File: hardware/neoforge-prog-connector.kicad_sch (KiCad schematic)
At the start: 1 part, among them J1 AES_CN5_PROG

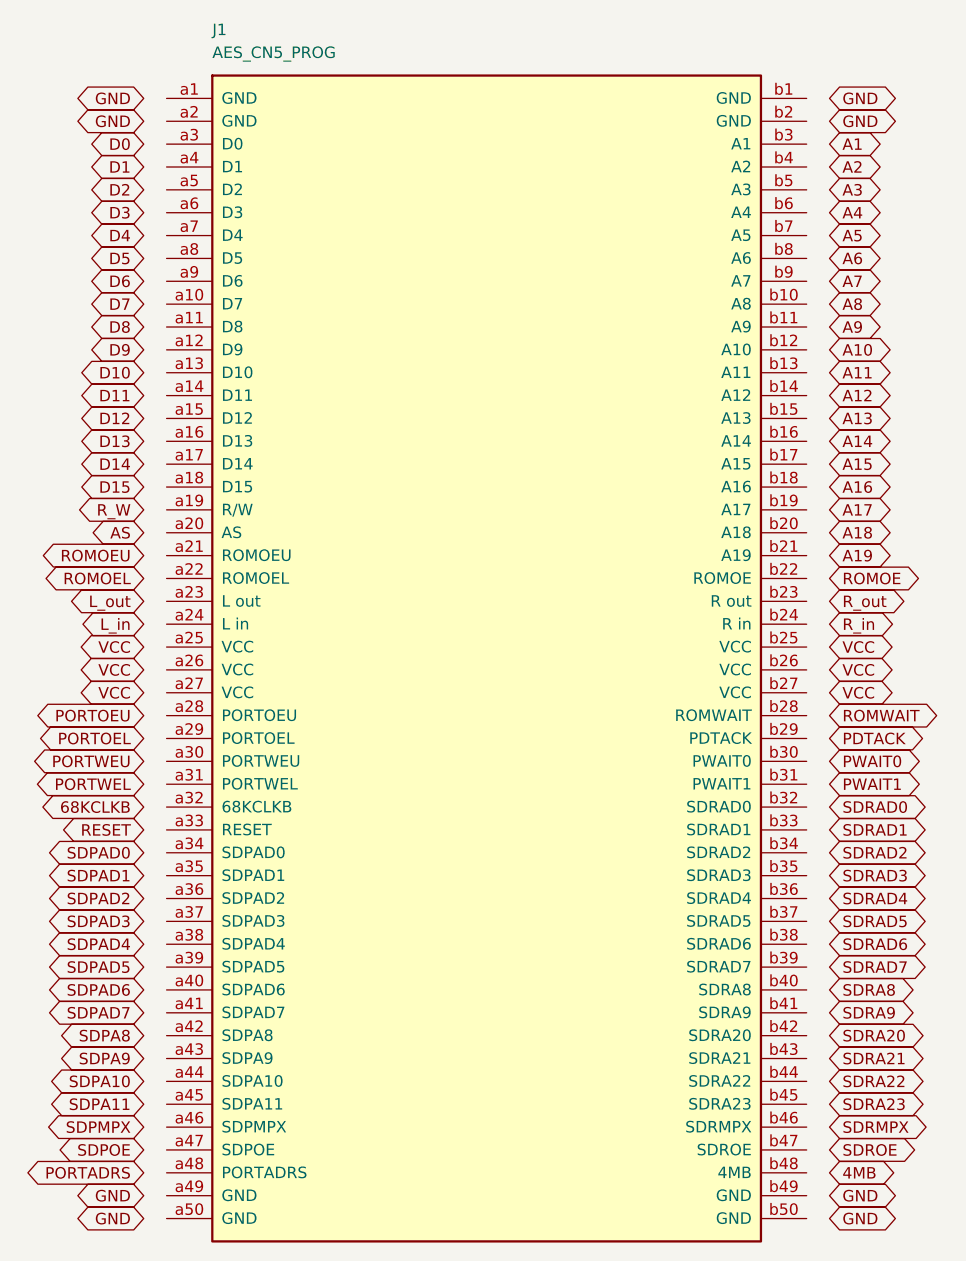
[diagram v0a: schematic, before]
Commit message: hardware: connector netlist verified 100/100
Exported from KiCad and checked back against the pinout CSV:

    J1 -> PROG CN5
      identified from the symbol's Value
      100/100 pins match the pinout
      no issues

The chain closes with nothing transcribed by hand: a CSV verified against
two independent sources, a symbol generated from it, a sheet generated
from it, KiCad's netlist exported from that, and the checker agreeing.

Three bugs were caught on the way and all three were in the tooling, not
the data - the Y-axis inversion between symbol and sheet space, an empty
lib_symbols that rendered a placeholder, and a label offset that produced
a sheet which looked correct and connected nothing. The last is the one
netcheck exists for.

Roadmap: Phase 7's connector item is electrically done, mechanically
open. The footprint still needs measuring off a real cartridge.
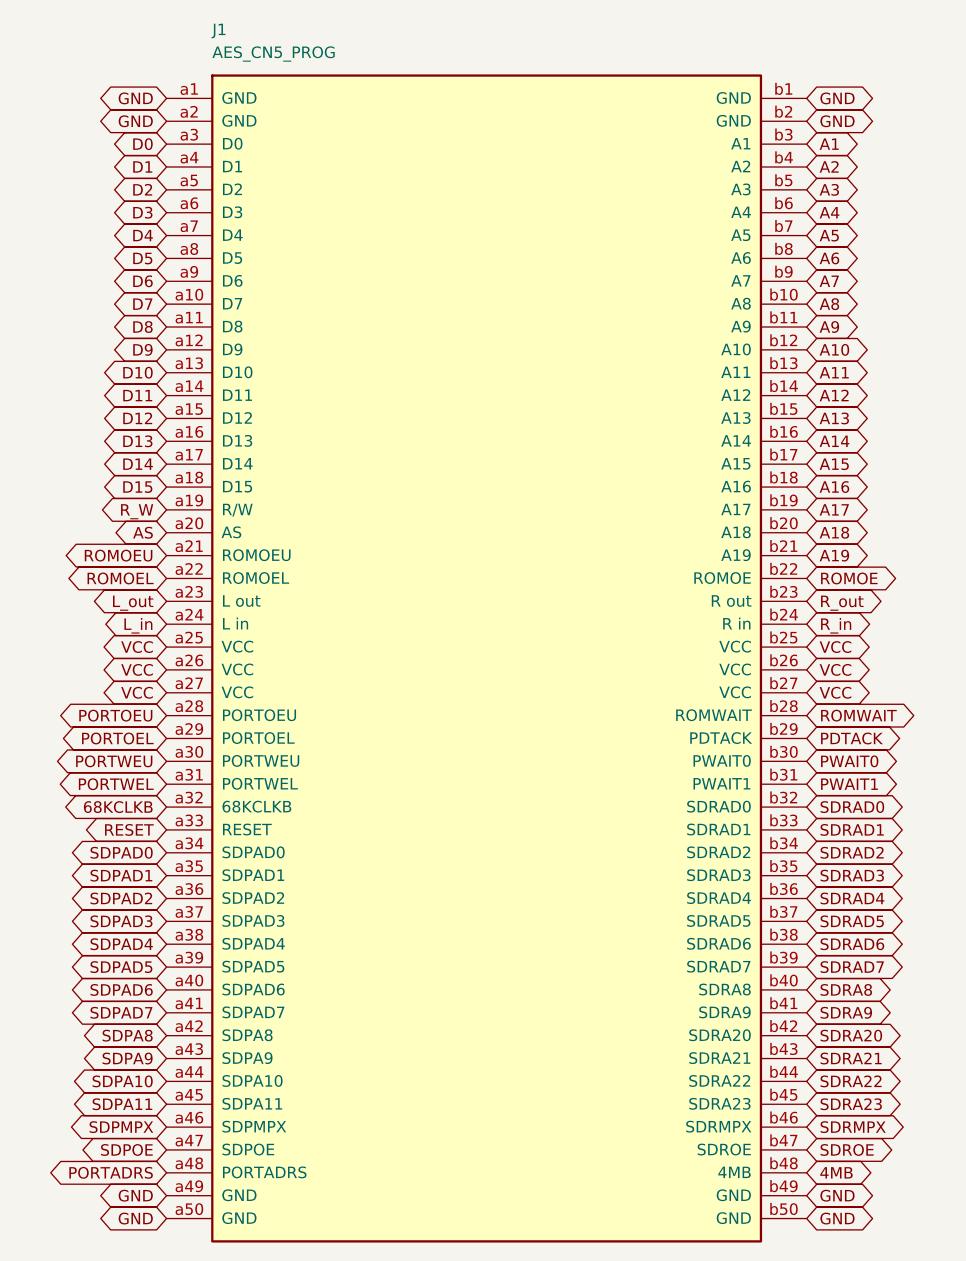
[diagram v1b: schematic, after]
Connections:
- net 4MB: now also J1.b48 (4MB)
- net 68KCLKB: now also J1.a32 (68KCLKB)
- net A1: now also J1.b3 (A1)
- net A10: now also J1.b12 (A10)
- net A11: now also J1.b13 (A11)
- net A12: now also J1.b14 (A12)
- net A13: now also J1.b15 (A13)
- net A14: now also J1.b16 (A14)
- net A15: now also J1.b17 (A15)
- net A16: now also J1.b18 (A16)
- net A17: now also J1.b19 (A17)
- net A18: now also J1.b20 (A18)
- net A19: now also J1.b21 (A19)
- net A2: now also J1.b4 (A2)
- net A3: now also J1.b5 (A3)
- net A4: now also J1.b6 (A4)
- net A5: now also J1.b7 (A5)
- net A6: now also J1.b8 (A6)
- net A7: now also J1.b9 (A7)
- net A8: now also J1.b10 (A8)
- net A9: now also J1.b11 (A9)
- net AS: now also J1.a20 (AS)
- net D0: now also J1.a3 (D0)
- net D1: now also J1.a4 (D1)
- net D10: now also J1.a13 (D10)
- net D11: now also J1.a14 (D11)
- net D12: now also J1.a15 (D12)
- net D13: now also J1.a16 (D13)
- net D14: now also J1.a17 (D14)
- net D15: now also J1.a18 (D15)
- net D2: now also J1.a5 (D2)
- net D3: now also J1.a6 (D3)
- net D4: now also J1.a7 (D4)
- net D5: now also J1.a8 (D5)
- net D6: now also J1.a9 (D6)
- net D7: now also J1.a10 (D7)
- net D8: now also J1.a11 (D8)
- net D9: now also J1.a12 (D9)
- net GND: now also J1.a1 (GND), J1.a2 (GND), J1.a49 (GND), J1.a50 (GND), J1.b1 (GND), J1.b2 (GND), J1.b49 (GND), J1.b50 (GND)
- net L_in: now also J1.a24 (L in)
- net L_out: now also J1.a23 (L out)
- net PDTACK: now also J1.b29 (PDTACK)
- net PORTADRS: now also J1.a48 (PORTADRS)
- net PORTOEL: now also J1.a29 (PORTOEL)
- net PORTOEU: now also J1.a28 (PORTOEU)
- net PORTWEL: now also J1.a31 (PORTWEL)
- net PORTWEU: now also J1.a30 (PORTWEU)
- net PWAIT0: now also J1.b30 (PWAIT0)
- net PWAIT1: now also J1.b31 (PWAIT1)
- net RESET: now also J1.a33 (RESET)
- net ROMOE: now also J1.b22 (ROMOE)
- net ROMOEL: now also J1.a22 (ROMOEL)
- net ROMOEU: now also J1.a21 (ROMOEU)
- net ROMWAIT: now also J1.b28 (ROMWAIT)
- net R_W: now also J1.a19 (R/W)
- net R_in: now also J1.b24 (R in)
- net R_out: now also J1.b23 (R out)
- net SDPA10: now also J1.a44 (SDPA10)
- net SDPA11: now also J1.a45 (SDPA11)
- net SDPA8: now also J1.a42 (SDPA8)
- net SDPA9: now also J1.a43 (SDPA9)
- net SDPAD0: now also J1.a34 (SDPAD0)
- net SDPAD1: now also J1.a35 (SDPAD1)
- net SDPAD2: now also J1.a36 (SDPAD2)
- net SDPAD3: now also J1.a37 (SDPAD3)
- net SDPAD4: now also J1.a38 (SDPAD4)
- net SDPAD5: now also J1.a39 (SDPAD5)
- net SDPAD6: now also J1.a40 (SDPAD6)
- net SDPAD7: now also J1.a41 (SDPAD7)
- net SDPMPX: now also J1.a46 (SDPMPX)
- net SDPOE: now also J1.a47 (SDPOE)
- net SDRA20: now also J1.b42 (SDRA20)
- net SDRA21: now also J1.b43 (SDRA21)
- net SDRA22: now also J1.b44 (SDRA22)
- net SDRA23: now also J1.b45 (SDRA23)
- net SDRA8: now also J1.b40 (SDRA8)
- net SDRA9: now also J1.b41 (SDRA9)
- net SDRAD0: now also J1.b32 (SDRAD0)
- net SDRAD1: now also J1.b33 (SDRAD1)
- net SDRAD2: now also J1.b34 (SDRAD2)
- net SDRAD3: now also J1.b35 (SDRAD3)
- net SDRAD4: now also J1.b36 (SDRAD4)
- net SDRAD5: now also J1.b37 (SDRAD5)
- net SDRAD6: now also J1.b38 (SDRAD6)
- net SDRAD7: now also J1.b39 (SDRAD7)
- net SDRMPX: now also J1.b46 (SDRMPX)
- net SDROE: now also J1.b47 (SDROE)
- net VCC: now also J1.a25 (VCC), J1.a26 (VCC), J1.a27 (VCC), J1.b25 (VCC), J1.b26 (VCC), J1.b27 (VCC)
